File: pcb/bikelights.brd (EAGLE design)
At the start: 53.3 x 59.7 mm, 8 parts, among them J1 COMPUTER-PERIPHERAL-POWERRA

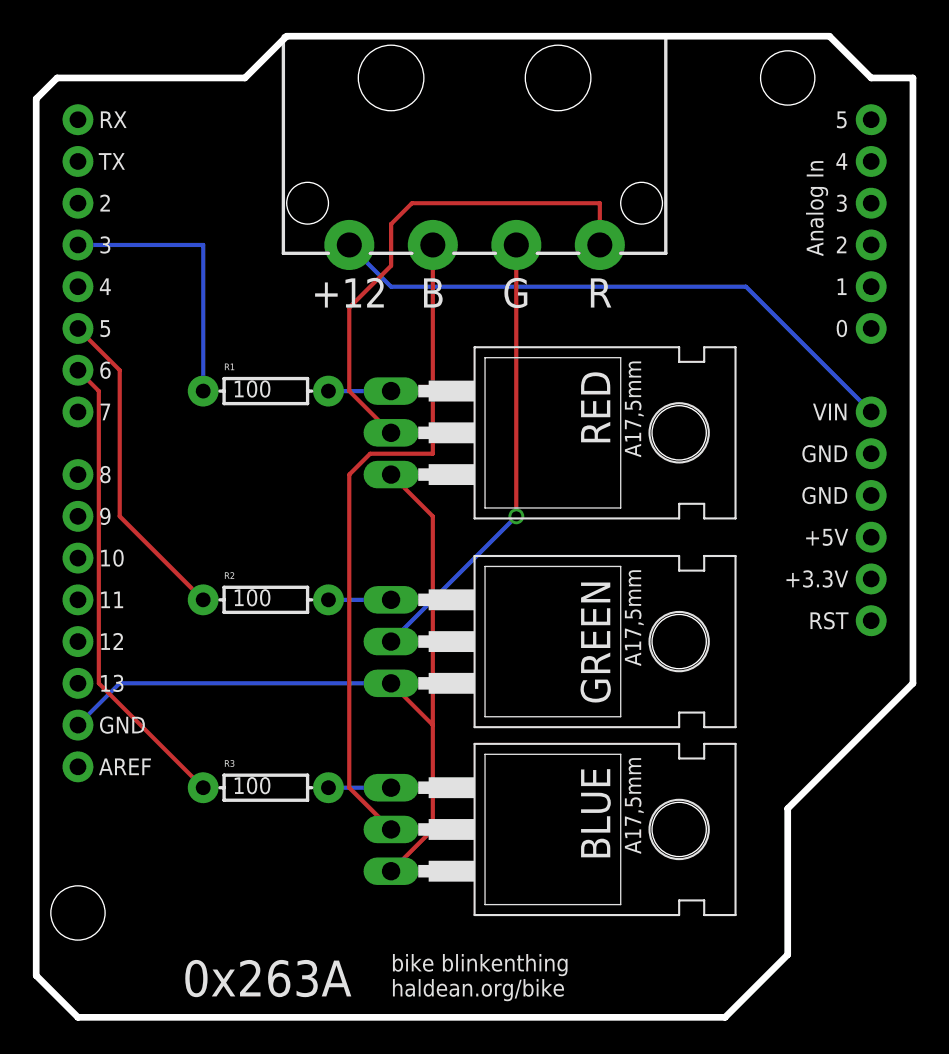
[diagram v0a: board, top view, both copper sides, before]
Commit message: New PCB for blinkenthing B.
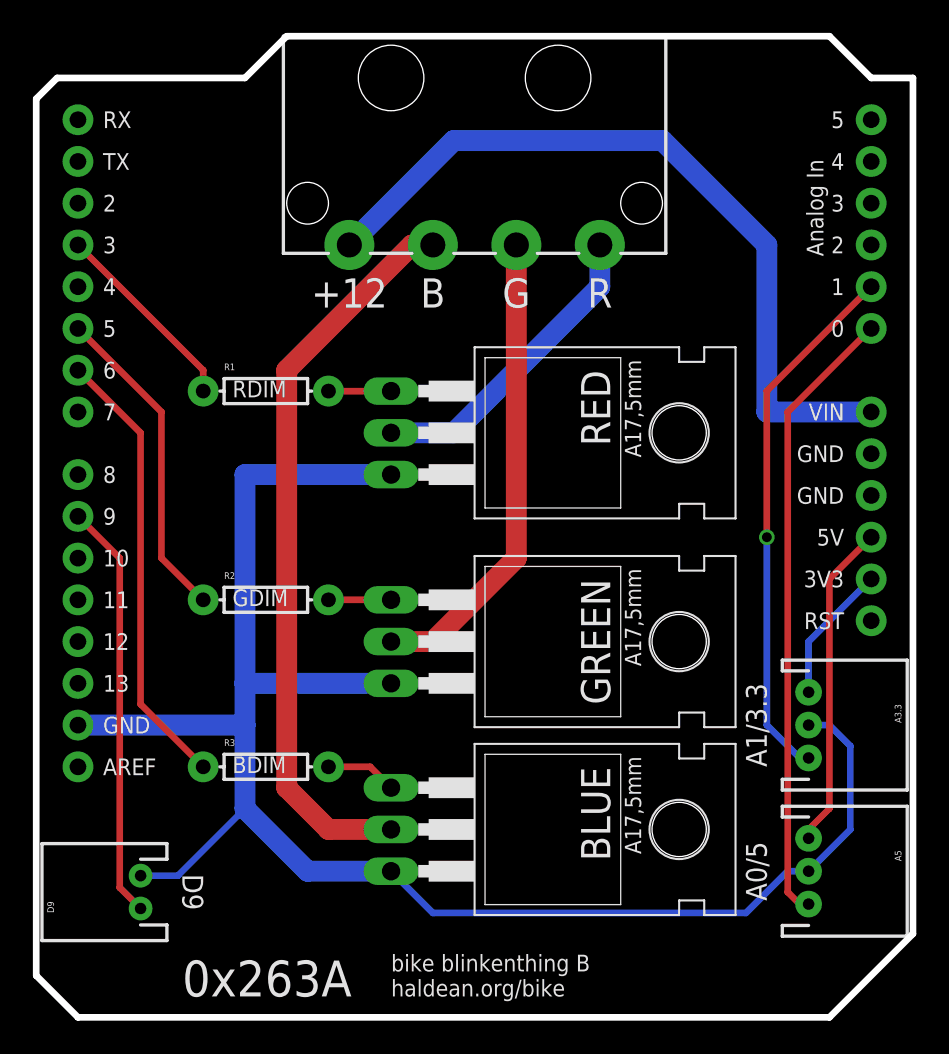
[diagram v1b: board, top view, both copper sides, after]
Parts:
- added A3.3, A5: (no value), SparkFun-Connectors:JST-3-PTH
- added D9: M02JST-PTH-2, SparkFun-Connectors:JST-2-PTH
- R1: value 100 -> RDIM
- R2: value 100 -> GDIM
- R3: value 100 -> BDIM
- SHIELD: value ARDUINO_SHIELDLABEL -> ARDUINO_SHIELDNOHOLES; device SparkFun-Boards:DUEMILANOVE_SHIELD -> SparkFun-Boards:DUEMILANOVE_SHIELD_NOHOLES
- moved R3 1.27 mm to (19.1, 31.8)
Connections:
- new net N$12: A5.1, SHIELD.5V
- new net N$13: D9.1, SHIELD.D9
- new net N$14: A5.3, SHIELD.A0
- new net N$15: A3.3.3, SHIELD.A1
- new net N$16: A3.3.1, SHIELD.3.3V
- net N$4: now also A3.3.2, A5.2, D9.2
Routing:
- net N$4: track 49.9 -> 106.0 mm
- net N$14: track 0.00 -> 38.0 mm
- net N$15: track 0.00 -> 32.7 mm, vias 0 -> 1
- net N$13: track 0.00 -> 25.4 mm
- net N$12: track 0.00 -> 19.9 mm
- net N$7: track 30.6 -> 18.9 mm
- net N$8: track 36.0 -> 47.2 mm
- net N$16: track 0.00 -> 8.47 mm
- net N$1: track 16.5 -> 12.0 mm
- net N$5: track 40.9 -> 44.8 mm
- net N$6: track 27.3 -> 28.8 mm, vias 1 -> 0
- net N$10: track 28.6 -> 27.3 mm
- net N$3: track 3.81 -> 4.34 mm
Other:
- outline, holes or cut-outs redrawn
- board text added: "A0/5"
- board text added: "A1/3.3"
- board text added: "D9"
- board text added: "bike blinkenthing B haldean.org/bike"
- board text removed: "bike blinkenthing haldean.org/bike"
